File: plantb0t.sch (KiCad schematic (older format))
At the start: 32 parts

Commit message: Updating a lot of stuff...
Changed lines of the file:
@@
 LIBS:valves
 LIBS:kookie_power
-LIBS:kookie_logic
 LIBS:kookie_mcu
+LIBS:kookie_sensors
 LIBS:ESP8266
-LIBS:kookie_sensors
 LIBS:plantb0t-cache
 EELAYER 25 0
@@
 	2350 7350 2350 7450
 Wire Wire Line
-	2350 4650 2350 5250
-Wire Wire Line
-	2350 5250 2350 5550
+	2350 4650 2350 5550
 Wire Wire Line
 	3050 5050 3000 5050
 Wire Wire Line
-	4400 4650 4400 5150
-Wire Wire Line
-	4400 5150 4400 5250
+	4400 4650 4400 5250
 Wire Wire Line
 	3250 6150 3800 6150
@@
 	650  2650 650  4150
 Wire Wire Line
-	9350 5100 9500 5100
-Wire Wire Line
-	9500 5100 9800 5100
-Wire Wire Line
-	9800 5100 9900 5100
+	9350 5100 9900 5100
 Wire Wire Line
 	9700 5200 9350 5200
 Wire Wire Line
-	10200 5250 10200 5500
-Wire Wire Line
-	10200 5500 10200 5600
-Wire Wire Line
-	7950 4100 7950 4700
-Wire Wire Line
-	7950 4700 7950 5200
-Wire Wire Line
-	7950 5200 7950 5850
+	10200 5250 10200 5600
+Wire Wire Line
+	7950 4100 7950 5850
 Wire Wire Line
 	7950 5200 8450 5200
@@
 Connection ~ 7950 4700
 Wire Wire Line
-	9500 4450 9600 4450
-Wire Wire Line
-	9600 4450 9700 4450
-Wire Wire Line
-	8750 4000 8950 4000
-Wire Wire Line
-	8950 4000 9200 4000
+	9500 4450 9700 4450
+Wire Wire Line
+	8750 4000 9200 4000
 Wire Wire Line
 	8950 4000 8950 4450
@@
 	8950 4450 9200 4450
 Wire Wire Line
-	7950 4100 9050 4100
-Wire Wire Line
-	9050 4100 9200 4100
+	7950 4100 9200 4100
 Wire Wire Line
 	9050 4100 9050 4200
@@
 Connection ~ 8950 4000
 Wire Wire Line
-	10400 4700 10400 4450
-Wire Wire Line
-	10400 4450 10400 4100
-Wire Wire Line
-	10000 4450 10400 4450
-Wire Wire Line
-	10400 4450 10700 4450
+	10400 4700 10400 4100
+Wire Wire Line
+	10000 4450 10700 4450
 Wire Notes Line
 	7600 3550 10950 3550
@@
 	8300 3850 8300 4200
 Wire Wire Line
-	8300 4500 8300 5100
-Wire Wire Line
-	8300 5100 8300 5650
-Wire Wire Line
-	2150 5250 2350 5250
-Wire Wire Line
-	2350 5250 3050 5250
+	8300 4500 8300 5650
+Wire Wire Line
+	2150 5250 3050 5250
 Connection ~ 2350 5250
 Wire Wire Line
 	1200 6250 1450 6250
 Wire Wire Line
-	1200 6350 1350 6350
-Wire Wire Line
-	1350 6350 1450 6350
+	1200 6350 1450 6350
 Wire Wire Line
 	1650 1750 1800 1750
 Wire Wire Line
-	2300 1650 3000 1650
-Wire Wire Line
-	3000 1650 3150 1650
+	2300 1650 3150 1650
 Wire Wire Line
 	3200 4650 3300 4650
@@
 	5150 5400 5150 5650
 Wire Wire Line
-	5150 5650 5700 5650
-Wire Wire Line
-	5700 5650 6050 5650
-Wire Wire Line
-	6050 5650 6300 5650
-Wire Wire Line
-	6300 5650 6550 5650
+	5150 5650 6550 5650
 Wire Wire Line
 	5550 5200 5700 5200
 Wire Wire Line
-	5700 5200 5700 5650
-Wire Wire Line
-	5700 5650 5700 5800
+	5700 5200 5700 5800
 Connection ~ 5700 5650
 Wire Wire Line
@@
 Connection ~ 6300 5650
 Wire Wire Line
-	5550 5000 6050 5000
-Wire Wire Line
-	6050 5000 6850 5000
-Wire Wire Line
-	5550 4900 6300 4900
-Wire Wire Line
-	6300 4900 6850 4900
+	5550 5000 6850 5000
+Wire Wire Line
+	5550 4900 6850 4900
 Wire Wire Line
 	6050 5250 6050 5000
@@
 	5550 4800 6550 4800
 Wire Wire Line
-	6550 4550 6550 4800
-Wire Wire Line
-	6550 4800 6550 5250
+	6550 4550 6550 5250
 Connection ~ 6550 4800
 Wire Wire Line
@@
 	9800 5950 9900 5950
 Wire Wire Line
-	9100 4700 9700 4700
-Wire Wire Line
-	9700 4700 10200 4700
-Wire Wire Line
-	10200 4700 10400 4700
+	9100 4700 10400 4700
 Wire Wire Line
 	10200 4700 10200 4850
@@
 Connection ~ 8600 4700
 Wire Wire Line
-	7950 4700 8600 4700
-Wire Wire Line
-	8600 4700 8800 4700
+	7950 4700 8800 4700
 Wire Wire Line
 	8600 4700 8600 4600
@@
 	6300 7000 6500 7000
 Wire Wire Line
-	6500 6700 6500 7000
-Wire Wire Line
-	6500 7000 6500 7200
+	6500 6700 6500 7200
 Wire Wire Line
 	6500 6700 6300 6700
@@
 	6000 3150 6000 3150
 Wire Wire Line
-	4150 3050 4450 3050
-Wire Wire Line
-	4450 3050 4800 3050
-Wire Wire Line
-	4450 2950 4450 3050
-Wire Wire Line
-	4450 3050 4450 3700
-Wire Wire Line
-	4450 3700 4450 3800
+	4150 3050 4800 3050
+Wire Wire Line
+	4450 2950 4450 3800
 Wire Wire Line
 	4800 3050 4800 2950
@@
 Connection ~ 4450 3700
 Wire Wire Line
-	4150 2550 5200 2550
-Wire Wire Line
-	5200 2550 5300 2550
+	4150 2550 5300 2550
 Connection ~ 5200 2550
 Wire Wire Line
-	4450 2450 4800 2450
-Wire Wire Line
-	4800 2450 5200 2450
-Wire Wire Line
-	5200 2450 5300 2450
+	4450 2450 5300 2450
 Connection ~ 5200 2450
 Wire Wire Line
@@
 	6300 3600 6650 3600
 Wire Wire Line
-	5200 2450 5200 2550
-Wire Wire Line
-	5200 2550 5200 3250
-Wire Wire Line
-	5200 3250 5200 3700
-Wire Wire Line
-	5200 3700 5200 3800
+	5200 2450 5200 3800
 Wire Wire Line
 	5900 3250 5900 3150

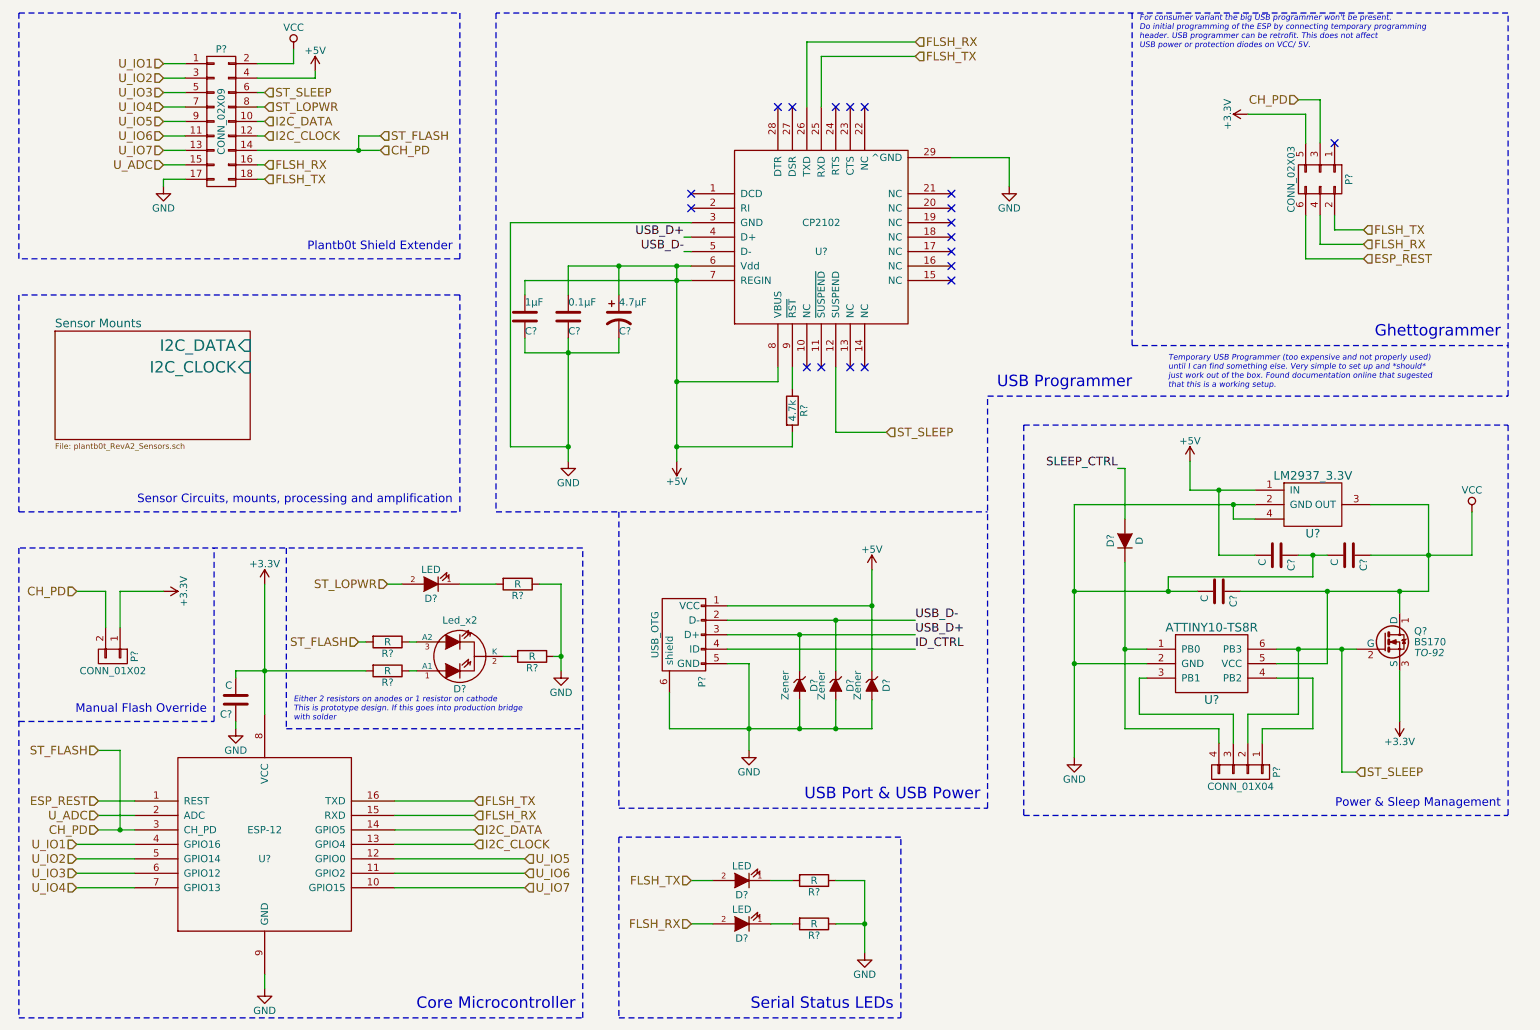
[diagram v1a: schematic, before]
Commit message: Loading in new kookie libs
Updating Bill of Material for capacitors
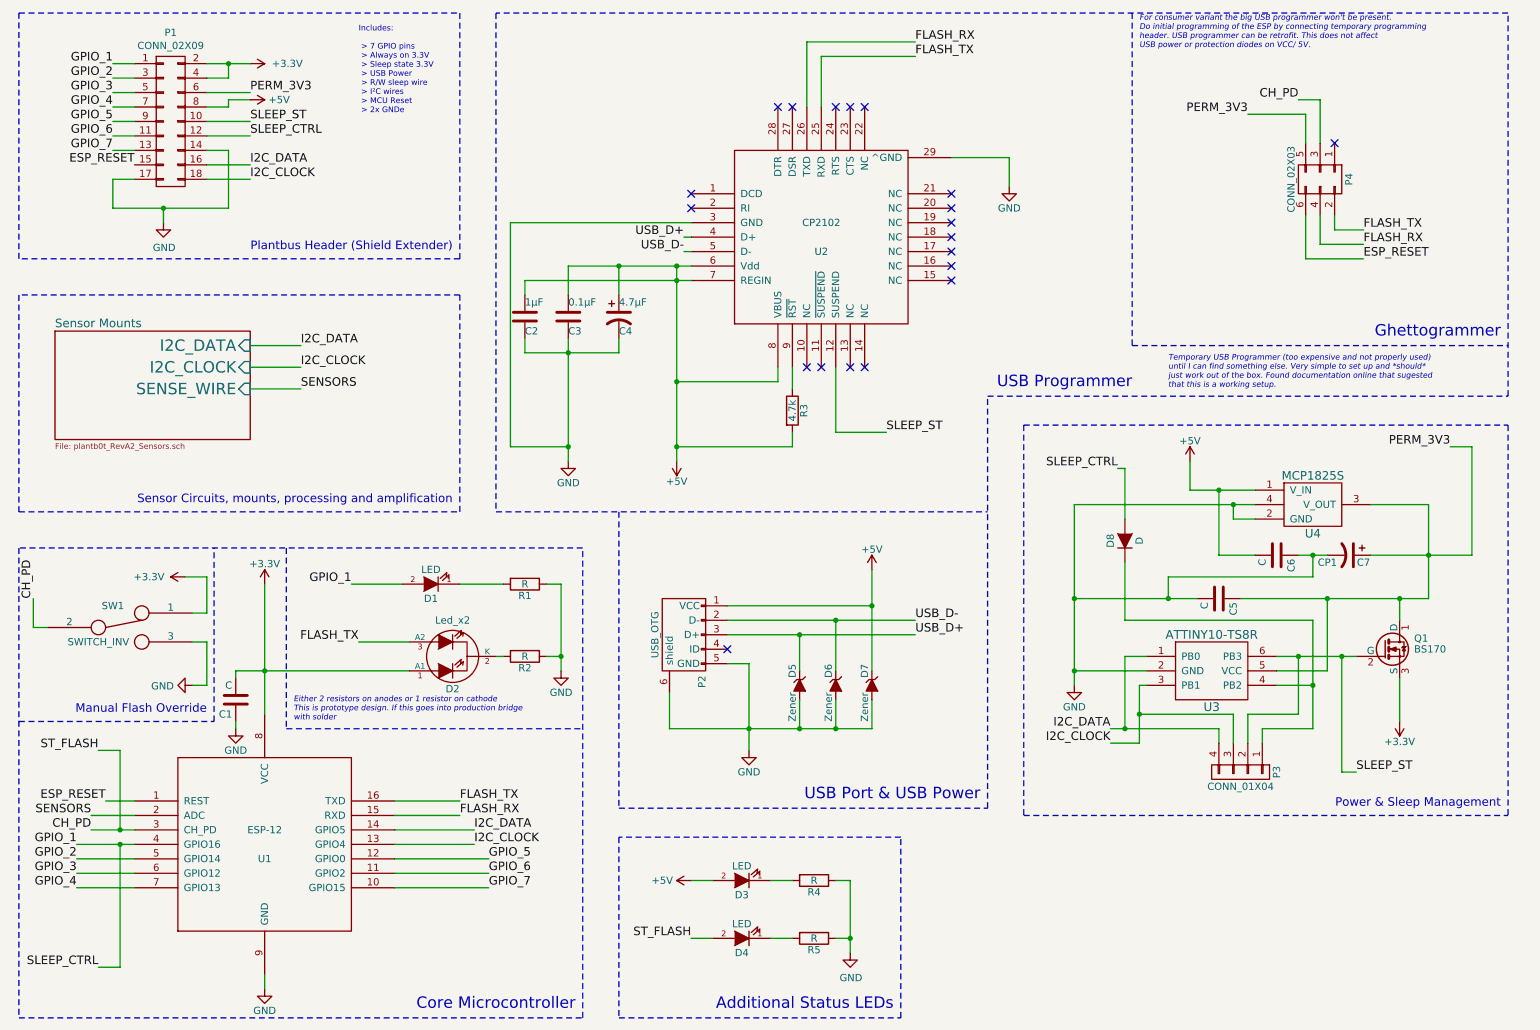
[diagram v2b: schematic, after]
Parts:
- removed C?: C, symbol C
- removed D? (x2): LED, symbol LED
- removed P?: CONN_02X09, symbol CONN_02X09
- removed P?: CONN_01X02, symbol CONN_01X02
- removed R? (x4): R, symbol R
- removed U?: LM2937_3.3V, symbol LM2937_3.3V
- added C7: CP1, symbol CP1
- added D3, D4: LED, symbol LED
- added P1: CONN_02X09, symbol CONN_02X09
- added R4, R5: R, symbol R
- added SW1: SWITCH_INV, symbol SWITCH_INV
- added U4: MCP1825S, symbol MCP1825S
- C1, C2, C3, C5, C6: renamed from C?; footprint (none) -> Capacitors_SMD:C_1206
- Q1: renamed from Q?; footprint TO-92 -> (none)
- gave numbers to parts that had none: 16
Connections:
- net FLSH_TX is gone; now on net FLASH_TX: P4.2 (P2), U1.16 (TXD), U2.25 (RXD)
- net ST_LOPWR is gone; now on net GPIO_1: D1.2 (A)
- net U_IO1 is gone; now on net GPIO_1: U1.4 (GPIO16)
- net +3V3: now also D2.1 (A1), P1.2 (P2), P1.4 (P4), SW1.1; no longer P4.5 (P5)
- net +5V: now also D3.2 (A), P1.8 (P8), U4.1 (V_IN)
- net CH_PD: now also D4.2 (A), SW1.2
- net GND: now also C7.2, P1.14 (P14), P1.17 (P17), R4.1, R5.1, SW1.3, U4.2 (GND), U4.4
- net I2C_CLOCK: now also P3.3 (P3), U3.3 (PB1), P1.18 (P18)
- net I2C_DATA: now also P3.4 (P4), U3.1 (PB0), P1.16 (P16)
- net at P3.1 (P1), U3.4 (PB2): now also D8.1 (K)
- net FLASH_TX: now reaches D2.3 (A2)
- net ESP_REST renamed ESP_RESET
- net ESP_RESET: now also P1.15 (P15)
- net FLSH_RX renamed FLASH_RX
- net ID_CTRL: no longer names the net of P2.4 (ID)
- net SLEEP_CTRL renamed GPIO_1
- net GPIO_1: now also P1.1 (P1), P1.12 (P12)
- net ST_SLEEP renamed SLEEP_ST
- net SLEEP_ST: now also P1.10 (P10)
- net U_ADC renamed SENSORS
- net U_IO2 renamed GPIO_2
- net GPIO_2: now also P1.3 (P3)
- net U_IO3 renamed GPIO_3
- net GPIO_3: now also P1.5 (P5)
- net U_IO4 renamed GPIO_4
- net GPIO_4: now also P1.7 (P7)
- net U_IO5 renamed GPIO_5
- net GPIO_5: now also P1.9 (P9)
- net U_IO6 renamed GPIO_6
- net GPIO_6: now also P1.11 (P11)
- net U_IO7 renamed GPIO_7
- net GPIO_7: now also P1.13 (P13)
- net VCC renamed PERM_3V3
- net PERM_3V3: now also P4.5 (P5), C7.1, P1.6 (P6), U4.3 (V_OUT)
- new net: D4.1 (K), R5.2
- new net: D3.1 (K), R4.2
- no-connect marks 19 -> 20
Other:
- note added: "Additional Status LEDs"
- note added: "Includes:\n\n > 7 GPIO pins\n > Always on 3.3V\n > Sleep state 3.3V\n > USB Power\n > R/W sleep wire\n > I²C wires\n > MCU Reset\n > 2x GNDe"
- note added: "Plantbus Header (Shield Extender)"
- note removed: "Plantb0t Shield Extender"
- note removed: "Serial Status LEDs"
- moved on the sheet: C5, D2, Q1, R1, R2, U3

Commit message: Starting Rev A2 board routing
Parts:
- removed C1, C5: C, Capacitors_SMD:C_1206, symbol C
- removed C7: CP1, symbol CP1
- removed D2: Led_x2, symbol Led_x2
- removed D8: D, symbol D
- removed P3: CONN_01X04, symbol CONN_01X04
- removed U3: ATTINY10-TS8R, symbol ATTINY10-TS8R
- removed U4: MCP1825S, symbol MCP1825S
- added C1, C6: 4.7µF, Capacitors_Tantalum_SMD:TantalC_SizeA_EIA-3216_HandSoldering, symbol CP1
- added R1, R2, R9: 10K, Resistors_SMD:R_0603, symbol R
- added R3: 220, Resistors_SMD:R_0603, symbol R
- added U12: LEDx2, base_types:SML-52, symbol LEDx2
- added U3: ZXCL5213V30H5CT-ND, TO_SOT_Packages_SMD:SOT-23-5, symbol ZXCL5213V30H5CT-ND
- C4: footprint (none) -> Capacitors_Tantalum_SMD:TantalC_SizeA_EIA-3216_HandSoldering
- C5: renamed from C6; value C -> 0.1µF
- D1, D3, D4: footprint (none) -> base_types:knightbright_3216
- D5, D6, D7: footprint (none) -> Diodes_SMD:SOD-323
- P1: footprint (none) -> Pin_Headers:Pin_Header_Straight_2x09
- P2: footprint (none) -> Connect:USB_Micro-B
- P3: renamed from P4; footprint (none) -> Pin_Headers:Pin_Header_Straight_2x03
- Q1: footprint (none) -> TO_SOT_Packages_SMD:SOT-23_Handsoldering
- R4: renamed from R1; value R -> 220; footprint (none) -> Resistors_SMD:R_0603
- R5: renamed from R2; value R -> 220; footprint (none) -> Resistors_SMD:R_0603
- R6: renamed from R3; footprint (none) -> Resistors_SMD:R_0603
- R7: renamed from R4; value R -> 220; footprint (none) -> Resistors_SMD:R_0603
- R8: renamed from R5; value R -> 220; footprint (none) -> Resistors_SMD:R_0603
- SW1: footprint (none) -> Buttons_Switches_ThroughHole:SW_Micro_SPST_Angled
- U1: footprint (none) -> ESP8266:ESP-12
- U2: footprint (none) -> Housings_DFN_QFN:QFN-28-1EP_5x5mm_Pitch0.5mm
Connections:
- net +3V3: no longer U1.8 (VCC)
- net +5V: now also P1.10 (P10), U3.1 (V_IN), U3.3 (EN); no longer P1.8 (P8)
- net FLASH_TX: now also U12.1 (AN_A)
- net GND: now also P3.1 (P1), C1.2, C6.2, R3.1, R9.2, U3.2 (GND)
- net GPIO_1: no longer P1.12 (P12), U1.4 (GPIO16)
- net I2C_CLOCK: now also R2.2
- net I2C_DATA: now also R1.2
- net PERM_3V3: now also P1.8 (P8), U1.8 (VCC), C1.1, C6.1, R1.1, R2.1, U12.2 (AN_B), U3.4 (V_O)
- net SLEEP_ST: now also U2.11 (~SUSPEND); no longer P1.10 (P10), Q1.2 (G), U2.12 (SUSPEND)
- net at R5.2: now also U12.4 (KAT_B)
- new net: R3.2, U12.3 (KAT_A)
- new net SLEEP_CTRL: P1.12 (P12), Q1.2 (G), R9.1, U1.4 (GPIO16)
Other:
- note removed: "Either 2 resistors on anodes or 1 resistor on cathode\nThis is prototype design. If this goes into production bridge\nwith solder"
- moved on the sheet: D1, Q1, R4, R5
